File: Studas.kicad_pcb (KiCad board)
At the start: 2 copper layers, 101.1 x 97.9 mm, 29 parts, among them J1 MJ-4PP-9, SW10_L1 SW_Diode_Combined, SW11_L1 SW_Diode_Combined, SW12_L1 SW_Diode_Combined, SW13_L1 SW_Diode_Combined, SW14_L1 SW_Diode_Combined, SW15_L1 SW_Diode_Combined, SW16_L1 SW_Diode_Combined, SW17_L1 SW_Diode_Combined, SW1_L1 SW_Diode_Combined, SW2_L1 SW_Diode_Combined, SW3_L1 SW_Diode_Combined, SW4_L1 SW_Diode_Combined, SW5_L1 SW_Diode_Combined, SW6_L1 SW_Diode_Combined, SW7_L1 SW_Diode_Combined, SW8_L1 SW_Diode_Combined, SW9_L1 SW_Diode_Combined, U1 xiao-ble

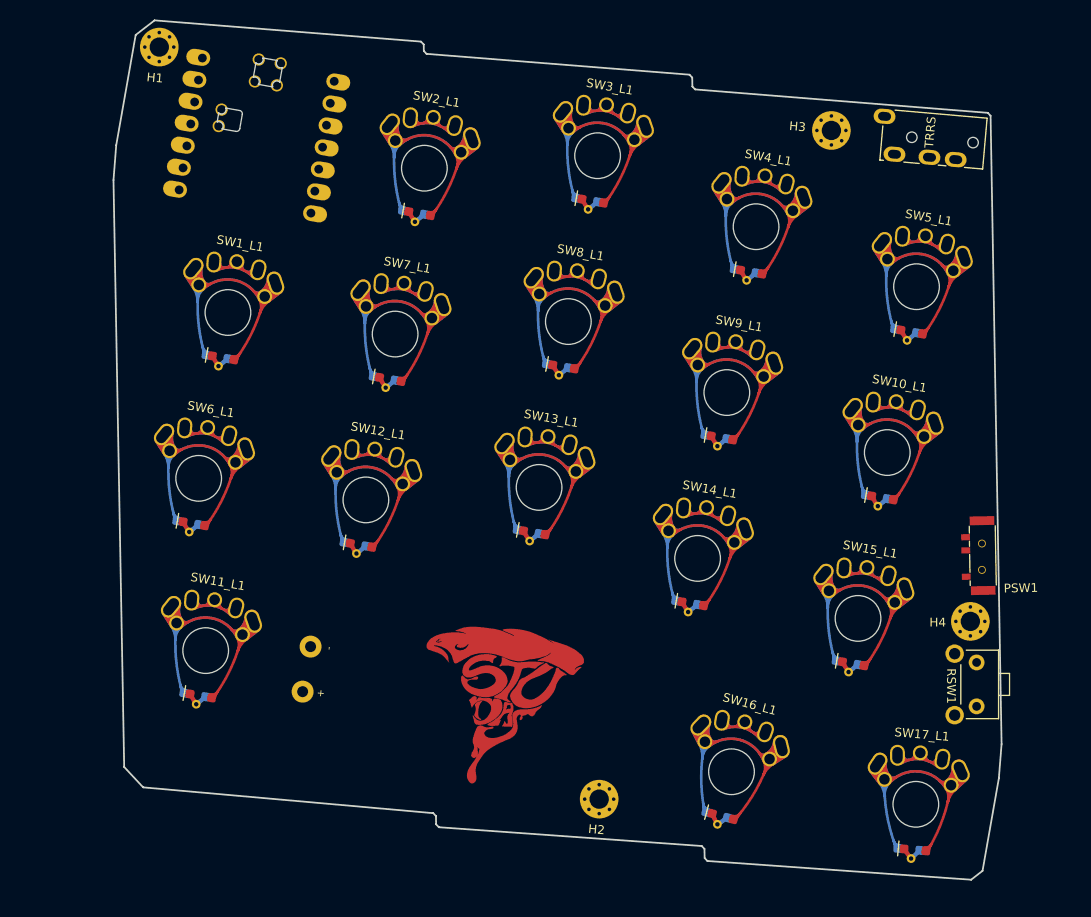
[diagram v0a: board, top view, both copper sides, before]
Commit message: Finished Routing - Ready to order
I FINALLY ROUTED THE BOARD :)

Added EVERY symbol/footprint used in the project.

There are some footprint warnings that I couldn't care less.

Suggestions for V1.2:

- Make Switch plate board 
- Add some teardrop pads
- Make copper traces "melt" (using round track plugin)
- Check for better placement of mounting holes
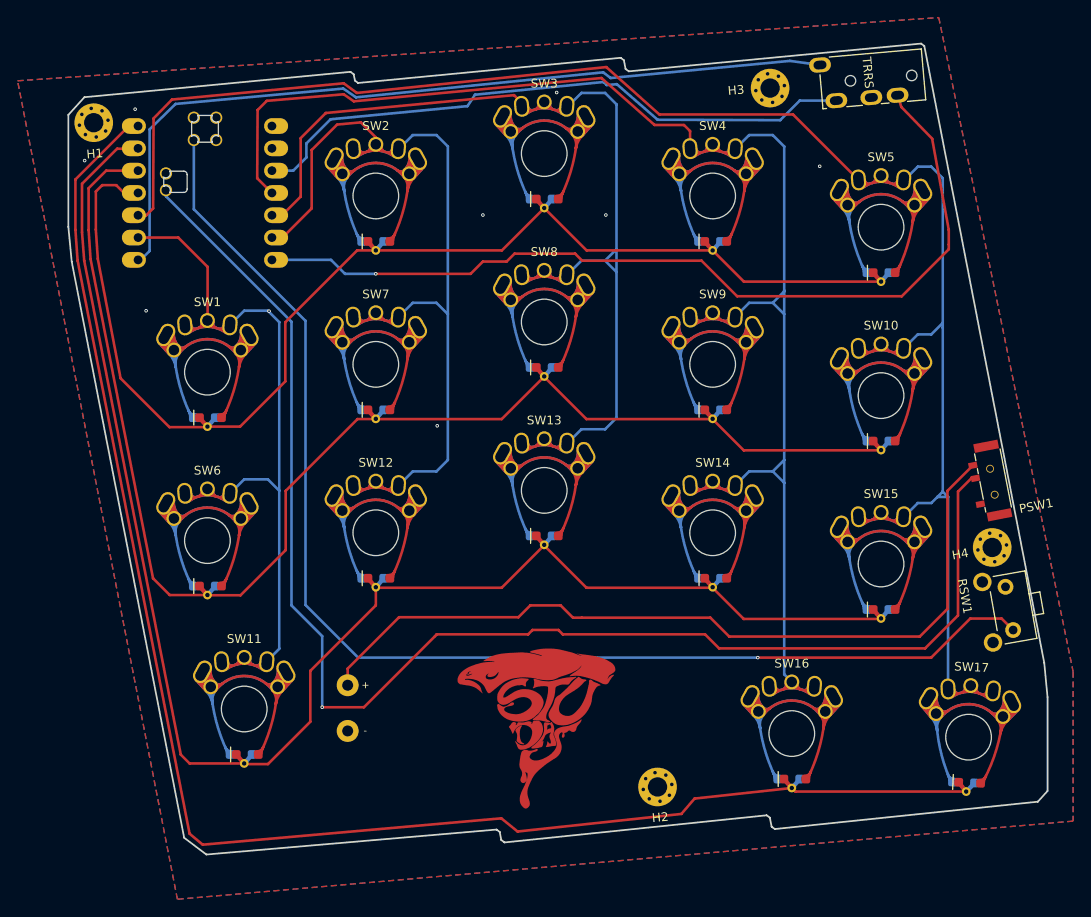
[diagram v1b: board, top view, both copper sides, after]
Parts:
- BAT+1, BATGND1: footprint TOTEMlib:BatteryPad -> STUDASlib:BatteryPad
- J1: footprint TOTEMlib:MJ-4PP-9_1side -> STUDASlib:MJ-4PP-9_1side
- PSW1: footprint TOTEMlib:MSK12C02 -> STUDASlib:MSK12C02
- RSW1: footprint TOTEMlib:SKHLLCA010 -> STUDASlib:SKHLLCA010
- SW1: renamed from SW1_L1; footprint TOTEMlib:SW_MX_GATLP_CHOC_reversible -> STUDASlib:SW_MX_GATLP_CHOC_reversible
- SW10: renamed from SW10_L1; footprint TOTEMlib:SW_MX_GATLP_CHOC_reversible -> STUDASlib:SW_MX_GATLP_CHOC_reversible
- SW11: renamed from SW11_L1; footprint TOTEMlib:SW_MX_GATLP_CHOC_reversible -> STUDASlib:SW_MX_GATLP_CHOC_reversible
- SW12: renamed from SW12_L1; footprint TOTEMlib:SW_MX_GATLP_CHOC_reversible -> STUDASlib:SW_MX_GATLP_CHOC_reversible
- SW13: renamed from SW13_L1; footprint TOTEMlib:SW_MX_GATLP_CHOC_reversible -> STUDASlib:SW_MX_GATLP_CHOC_reversible
- SW14: renamed from SW14_L1; footprint TOTEMlib:SW_MX_GATLP_CHOC_reversible -> STUDASlib:SW_MX_GATLP_CHOC_reversible
- SW15: renamed from SW15_L1; footprint TOTEMlib:SW_MX_GATLP_CHOC_reversible -> STUDASlib:SW_MX_GATLP_CHOC_reversible
- SW16: renamed from SW16_L1; footprint TOTEMlib:SW_MX_GATLP_CHOC_reversible -> STUDASlib:SW_MX_GATLP_CHOC_reversible
- SW17: renamed from SW17_L1; footprint TOTEMlib:SW_MX_GATLP_CHOC_reversible -> STUDASlib:SW_MX_GATLP_CHOC_reversible
- SW2: renamed from SW2_L1; footprint TOTEMlib:SW_MX_GATLP_CHOC_reversible -> STUDASlib:SW_MX_GATLP_CHOC_reversible
- SW3: renamed from SW3_L1; footprint TOTEMlib:SW_MX_GATLP_CHOC_reversible -> STUDASlib:SW_MX_GATLP_CHOC_reversible
- SW4: renamed from SW4_L1; footprint TOTEMlib:SW_MX_GATLP_CHOC_reversible -> STUDASlib:SW_MX_GATLP_CHOC_reversible
- SW5: renamed from SW5_L1; footprint TOTEMlib:SW_MX_GATLP_CHOC_reversible -> STUDASlib:SW_MX_GATLP_CHOC_reversible
- SW6: renamed from SW6_L1; footprint TOTEMlib:SW_MX_GATLP_CHOC_reversible -> STUDASlib:SW_MX_GATLP_CHOC_reversible
- SW7: renamed from SW7_L1; footprint TOTEMlib:SW_MX_GATLP_CHOC_reversible -> STUDASlib:SW_MX_GATLP_CHOC_reversible
- SW8: renamed from SW8_L1; footprint TOTEMlib:SW_MX_GATLP_CHOC_reversible -> STUDASlib:SW_MX_GATLP_CHOC_reversible
- SW9: renamed from SW9_L1; footprint TOTEMlib:SW_MX_GATLP_CHOC_reversible -> STUDASlib:SW_MX_GATLP_CHOC_reversible
- U1: footprint TOTEMlib:xiao-ble-smd-cutout -> STUDASlib:xiao-ble-smd-cutout
- moved H1 11.4 mm to (95.1, 51.3), turned to 10 degrees
- moved J1 10.6 mm to (189.7, 45.8), turned to -85 degrees
- moved BATGND1 10.5 mm to (124.0, 120.5), turned to -85 degrees
- moved SW17 9.72 mm to (194.7, 121.3), turned to -2.5 degrees
- moved RSW1 9.23 mm to (198.1, 106.8), turned to -80 degrees
- moved PSW1 9.03 mm to (199.5, 95.6), turned to -168.997 degrees
- moved U1 8.79 mm to (107.8, 59.3), turned to 0 degrees
- moved H4 8.78 mm to (197.4, 99.7), turned to 10 degrees
- moved H3 8.48 mm to (172.1, 47.3), turned to 10 degrees
- moved SW16 8.13 mm to (174.6, 120.9), turned to 0 degrees
- moved SW11 7.97 mm to (112.2, 118.1), turned to 0 degrees
- moved SW5 7.89 mm to (184.7, 63.2), turned to 0 degrees
- moved SW1 7.18 mm to (108.0, 79.7), turned to 0 degrees
- moved SW6 7.16 mm to (108.0, 98.9), turned to 0 degrees
- moved H2 6.79 mm to (159.3, 126.9), turned to 10 degrees
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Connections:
- net RX_L renamed RX
- net TX_L renamed TX
- net bat+_L renamed bat+
- net gnd_L renamed gnd
- net reset_L renamed reset
- net vbat_L renamed vbat
- net vcc_L renamed vcc
- SW1 pad 1: col1_L -> col1
- SW1 pad 3: row1_L -> row1
- SW10 pad 1: col5_L -> col5
- SW10 pad 3: row2_L -> row2
- SW11 pad 1: col1_L -> col1
- SW11 pad 3: row3_L -> row3
- SW12 pad 1: col2_L -> col2
- SW12 pad 3: row3_L -> row3
- SW13 pad 1: col3_L -> col3
- SW13 pad 3: row3_L -> row3
- SW14 pad 1: col4_L -> col4
- SW14 pad 3: row3_L -> row3
- SW15 pad 1: col5_L -> col5
- SW15 pad 3: row3_L -> row3
- SW16 pad 1: col4_L -> col4
- SW16 pad 3: row4_L -> row4
- SW17 pad 1: col5_L -> col5
- SW17 pad 3: row4_L -> row4
- SW2 pad 1: col2_L -> col2
- SW2 pad 3: row1_L -> row1
- SW3 pad 1: col3_L -> col3
- SW3 pad 3: row1_L -> row1
- SW4 pad 1: col4_L -> col4
- SW4 pad 3: row1_L -> row1
- SW5 pad 1: col5_L -> col5
- SW5 pad 3: row1_L -> row1
- SW6 pad 1: col1_L -> col1
- SW6 pad 3: row2_L -> row2
- SW7 pad 1: col2_L -> col2
- SW7 pad 3: row2_L -> row2
- SW8 pad 1: col3_L -> col3
- SW8 pad 3: row2_L -> row2
- SW9 pad 1: col4_L -> col4
- SW9 pad 3: row2_L -> row2
- U1 pad 1: row1_L -> row4
- U1 pad 10: col3_L -> col3
- U1 pad 11: col3_L -> col4
- U1 pad 2: row2_L -> row3
- U1 pad 3: row3_L -> row2
- U1 pad 4: row4_L -> row1
- U1 pad 5: col1_L -> col5
- U1 pad 6: col2_L -> col1
- U1 pad 9: col4_L -> col2
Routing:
- net row4: track 0.00 -> 176.1 mm
- net col5: track 0.00 -> 175.9 mm
- net row3: track 0.00 -> 172.7 mm
- net bat+: track 0.00 -> 161.9 mm, vias 0 -> 1
- net row2: track 0.00 -> 153.0 mm
- net col4: track 0.00 -> 150.1 mm
- net reset: track 0.00 -> 143.7 mm, vias 0 -> 1
- net row1: track 0.00 -> 133.6 mm
- net RX: track 0.00 -> 102.1 mm, vias 0 -> 1
- net col3: track 0.00 -> 96.1 mm
- net TX: track 0.00 -> 94.0 mm
- net vbat: track 0.00 -> 93.5 mm
- net col2: track 0.00 -> 78.7 mm
- net vcc: track 0.00 -> 71.1 mm
- net col1: track 0.00 -> 68.3 mm
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- added copper zone on B.Cu, net gnd
- added copper zone on F.Cu, net gnd
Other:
- board size 101.1 x 97.9 mm -> 111.5 x 92.3 mm
